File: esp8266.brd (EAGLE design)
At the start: 29.5 x 28.6 mm, 35 parts, among them IC1 74LVC1G08DBV, U1 FT232RL-BASICSSOP, U2 SPX3819M5-L33

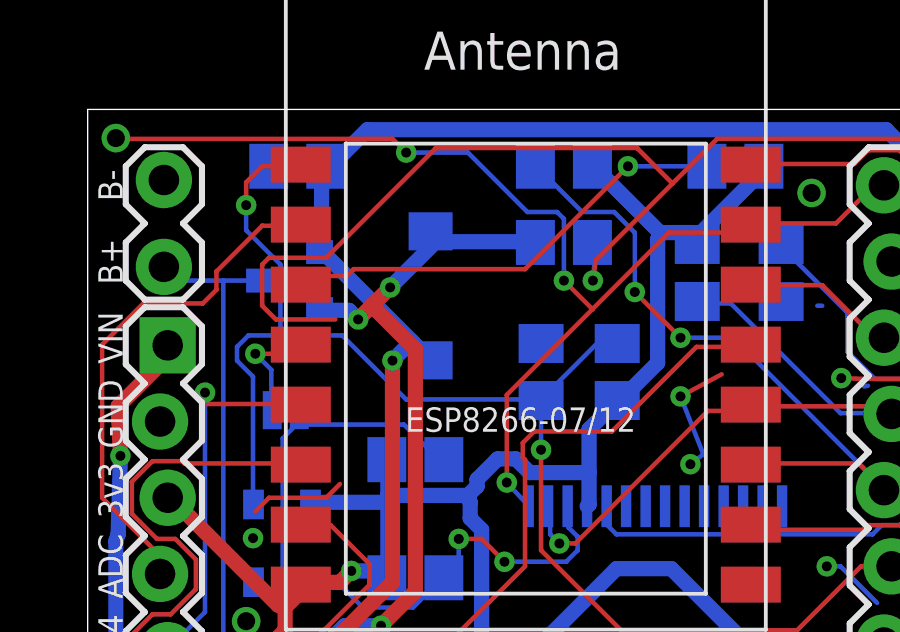
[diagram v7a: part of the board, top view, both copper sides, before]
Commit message: Remove unnecessary components
RTS had a capacitor that is not required per FTDI spec and is also not needed for this
circuit. There were also 2 10k pull-ups on the RTS.
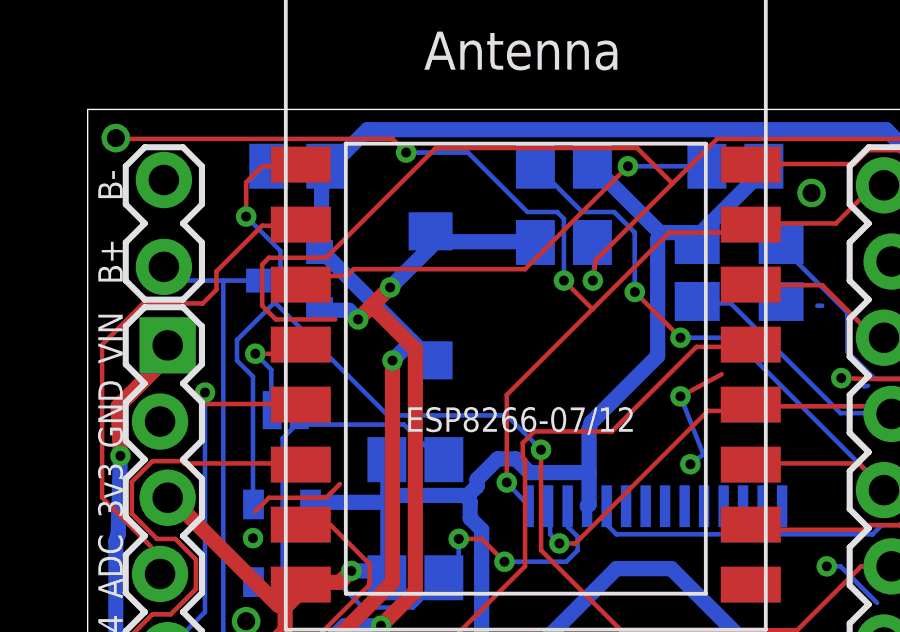
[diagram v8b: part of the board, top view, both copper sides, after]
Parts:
- removed C5: 470pF, rcl:C0805
- removed R1: 10k, resistor:R0805
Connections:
- net 3V3: no longer R1.1
- net GND: no longer C5.2
- net RTS: no longer C5.1, R1.2
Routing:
- net RTS: track 46.3 -> 42.0 mm
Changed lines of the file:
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@@
 <?xml version="1.0" encoding="utf-8"?>
 <!DOCTYPE eagle SYSTEM "eagle.dtd">
-<eagle version="7.4.0">
+<eagle version="7.3.0">
 <drawing>
 <settings>
@@
 <grid distance="0.025" unitdist="inch" unit="inch" style="dots" multiple="1" display="no" altdistance="0.01" altunitdist="inch" altunit="inch"/>
 <layers>
-<layer number="1" name="Top" color="4" fill="1" visible="no" active="yes"/>
+<layer number="1" name="Top" color="4" fill="1" visible="yes" active="yes"/>
 <layer number="16" name="Bottom" color="1" fill="1" visible="yes" active="yes"/>
 <layer number="17" name="Pads" color="2" fill="1" visible="no" active="yes"/>
@@
 <attribute name="VALUE" x="15.6845" y="54.4195" size="0.4064" layer="28" rot="MR90"/>
 </element>
-<element name="R1" library="resistor" package="R0805" value="10k" x="26.543" y="71.247" smashed="yes" rot="MR90">
-<attribute name="NAME" x="26.543" y="68.961" size="0.8128" layer="26" font="vector" rot="MR0" align="center"/>
-<attribute name="VALUE" x="24.003" y="70.612" size="1.27" layer="28" rot="MR90"/>
-</element>
-<element name="C5" library="rcl" package="C0805" value="470pF" x="24.003" y="71.247" smashed="yes" rot="MR90">
-<attribute name="NAME" x="24.003" y="73.533" size="0.8128" layer="26" font="vector" rot="MR0" align="center"/>
-<attribute name="VALUE" x="21.463" y="69.977" size="1.27" layer="28" rot="MR90"/>
-</element>
 <element name="C4" library="rcl" package="C0805" value="10uF" x="31.75" y="54.61" smashed="yes" rot="MR270">
 <attribute name="NAME" x="29.083" y="54.991" size="0.8128" layer="26" font="vector" rot="MR180"/>
@@
 <contactref element="U1" pad="26"/>
 <contactref element="U2" pad="2"/>
-<contactref element="C5" pad="2"/>
 <contactref element="C4" pad="2"/>
 <contactref element="IC1" pad="3"/>
@@
 <contactref element="ESP8266-07/12" pad="1"/>
 <contactref element="JP3" pad="2"/>
-<contactref element="R1" pad="2"/>
-<contactref element="C5" pad="1"/>
 <contactref element="IC1" pad="4"/>
-<wire x1="14.4018" y1="71.0946" x2="14.4018" y2="66.9036" width="0.1524" layer="16"/>
-<wire x1="13.8684" y1="71.628" x2="14.4018" y2="71.0946" width="0.1524" layer="16"/>
-<wire x1="13.8684" y1="72.0852" x2="13.8684" y2="71.628" width="0.1524" layer="16"/>
-<wire x1="14.2494" y1="72.4662" x2="13.8684" y2="72.0852" width="0.1524" layer="16"/>
-<wire x1="17.3736" y1="72.4662" x2="15.3162" y2="72.4662" width="0.1524" layer="16"/>
-<wire x1="15.3162" y1="72.4662" x2="14.2494" y2="72.4662" width="0.1524" layer="16"/>
-<wire x1="19.5072" y1="70.3326" x2="17.3736" y2="72.4662" width="0.1524" layer="16"/>
-<wire x1="24.003" y1="70.3326" x2="19.5072" y2="70.3326" width="0.1524" layer="16"/>
-<wire x1="14.4018" y1="66.9036" x2="14.417" y2="66.832" width="0.1524" layer="16"/>
-<wire x1="25.8318" y1="72.1614" x2="26.5176" y2="72.1614" width="0.1524" layer="16"/>
-<wire x1="24.003" y1="70.3326" x2="25.8318" y2="72.1614" width="0.1524" layer="16"/>
-<wire x1="26.5176" y1="72.1614" x2="26.543" y2="72.197" width="0.1524" layer="16"/>
-<wire x1="24.003" y1="70.3326" x2="24.003" y2="70.297" width="0.1524" layer="16"/>
 <wire x1="14.7066" y1="78.105" x2="15.9258" y2="78.105" width="0.1524" layer="1"/>
 <wire x1="14.1732" y1="77.5716" x2="14.7066" y2="78.105" width="0.1524" layer="1"/>
-<wire x1="14.1732" y1="76.8096" x2="14.1732" y2="77.5716" width="0.1524" layer="1"/>
-<wire x1="14.1732" y1="75.9714" x2="14.1732" y2="76.8096" width="0.1524" layer="16"/>
-<wire x1="15.3162" y1="74.8284" x2="14.1732" y2="75.9714" width="0.1524" layer="16"/>
-<wire x1="15.3162" y1="72.4662" x2="15.3162" y2="74.8284" width="0.1524" layer="16"/>
+<wire x1="14.1732" y1="76.4286" x2="14.1732" y2="77.5716" width="0.1524" layer="1"/>
 <wire x1="15.9258" y1="78.105" x2="15.995" y2="78.16" width="0.1524" layer="1"/>
 <wire x1="32.5374" y1="62.6364" x2="34.671" y2="64.77" width="0.1524" layer="1"/>
@@
 <wire x1="24.003" y1="65.3034" x2="26.67" y2="62.6364" width="0.1524" layer="1"/>
 <wire x1="24.003" y1="68.6562" x2="24.003" y2="65.3034" width="0.1524" layer="1"/>
-<wire x1="24.003" y1="70.297" x2="24.003" y2="68.6562" width="0.1524" layer="16"/>
-<via x="14.1732" y="76.8096" extent="1-16" drill="0.3302"/>
+<wire x1="34.671" y1="64.77" x2="35.687" y2="64.77" width="0.1524" layer="1"/>
+<wire x1="14.4018" y1="71.0946" x2="14.4018" y2="66.9036" width="0.1524" layer="16"/>
+<wire x1="13.8684" y1="71.628" x2="14.4018" y2="71.0946" width="0.1524" layer="16"/>
+<wire x1="13.8684" y1="72.3138" x2="13.8684" y2="71.628" width="0.1524" layer="16"/>
+<wire x1="15.3162" y1="73.7616" x2="15.1257" y2="73.5711" width="0.1524" layer="16"/>
+<wire x1="15.1257" y1="73.5711" x2="13.8684" y2="72.3138" width="0.1524" layer="16"/>
+<wire x1="15.3162" y1="75.2856" x2="15.3162" y2="73.7616" width="0.1524" layer="16"/>
+<wire x1="14.1732" y1="76.4286" x2="15.3162" y2="75.2856" width="0.1524" layer="16"/>
+<wire x1="14.4018" y1="66.9036" x2="14.417" y2="66.832" width="0.1524" layer="16"/>
+<wire x1="18.8976" y1="69.7992" x2="15.1257" y2="73.5711" width="0.1524" layer="16"/>
+<wire x1="22.86" y1="69.7992" x2="18.8976" y2="69.7992" width="0.1524" layer="16"/>
+<wire x1="24.003" y1="68.6562" x2="22.86" y2="69.7992" width="0.1524" layer="16"/>
+<via x="14.1732" y="76.4286" extent="1-16" drill="0.3302"/>
 <via x="24.003" y="68.6562" extent="1-16" drill="0.3302"/>
-<wire x1="34.671" y1="64.77" x2="35.687" y2="64.77" width="0.1524" layer="1"/>
 </signal>
 <signal name="VRIN" class="1">
@@
 <contactref element="ESP8266-07/12" pad="8"/>
 <contactref element="U2" pad="5"/>
-<contactref element="R1" pad="1"/>
 <contactref element="R10" pad="2"/>
 <contactref element="R3" pad="2"/>
@@
 <wire x1="29.2608" y1="75.5142" x2="29.21" y2="75.499" width="0.508" layer="16"/>
 <wire x1="31.3944" y1="78.105" x2="31.43" y2="78.105" width="0.508" layer="16"/>
-<wire x1="27.9654" y1="75.8952" x2="25.7556" y2="78.105" width="0.508" layer="16"/>
-<wire x1="29.0322" y1="75.8952" x2="27.9654" y2="75.8952" width="0.508" layer="16"/>
-<wire x1="25.7556" y1="78.105" x2="25.715" y2="78.105" width="0.508" layer="16"/>
-<wire x1="29.0322" y1="75.8952" x2="29.21" y2="75.499" width="0.508" layer="16"/>
 <wire x1="18.8976" y1="68.2752" x2="18.8976" y2="67.1322" width="0.508" layer="16"/>
 <wire x1="18.8976" y1="67.1322" x2="18.8976" y2="66.9036" width="0.508" layer="16"/>
@@
 <wire x1="25.6032" y1="69.342" x2="25.6032" y2="67.8942" width="0.508" layer="16"/>
 <wire x1="25.6032" y1="67.8942" x2="25.6032" y2="66.8274" width="0.508" layer="16"/>
-<wire x1="26.5176" y1="70.2564" x2="25.6032" y2="69.342" width="0.508" layer="16"/>
 <wire x1="25.6032" y1="66.8274" x2="25.538" y2="66.775" width="0.508" layer="16"/>
-<wire x1="26.5176" y1="70.2564" x2="26.543" y2="70.297" width="0.508" layer="16"/>
-<wire x1="27.8892" y1="71.5518" x2="27.8892" y2="75.6666" width="0.508" layer="16"/>
-<wire x1="26.7462" y1="70.4088" x2="27.8892" y2="71.5518" width="0.508" layer="16"/>
-<wire x1="27.8892" y1="75.6666" x2="27.9654" y2="75.8952" width="0.508" layer="16"/>
-<wire x1="26.7462" y1="70.4088" x2="26.543" y2="70.297" width="0.508" layer="16"/>
 <wire x1="14.6304" y1="61.7982" x2="14.6304" y2="60.0456" width="0.508" layer="1"/>
 <wire x1="15.4686" y1="62.6364" x2="14.6304" y2="61.7982" width="0.508" layer="1"/>
@@
 <wire x1="22.0218" y1="57.7596" x2="22.0218" y2="65.9892" width="0.508" layer="16"/>
 <wire x1="21.6408" y1="66.9036" x2="21.5646" y2="67.1322" width="0.508" layer="16"/>
+<wire x1="27.9654" y1="75.8952" x2="25.7556" y2="78.105" width="0.508" layer="16"/>
+<wire x1="29.0322" y1="75.8952" x2="27.9654" y2="75.8952" width="0.508" layer="16"/>
+<wire x1="25.7556" y1="78.105" x2="25.715" y2="78.105" width="0.508" layer="16"/>
+<wire x1="29.0322" y1="75.8952" x2="29.21" y2="75.499" width="0.508" layer="16"/>
+<wire x1="27.8892" y1="71.7804" x2="27.8892" y2="75.6666" width="0.508" layer="16"/>
+<wire x1="25.6794" y1="69.5706" x2="27.8892" y2="71.7804" width="0.508" layer="16"/>
+<wire x1="27.8892" y1="75.6666" x2="27.9654" y2="75.8952" width="0.508" layer="16"/>
+<wire x1="25.6794" y1="69.5706" x2="25.6032" y2="69.342" width="0.508" layer="16"/>
 </signal>
 <signal name="RXLED">
